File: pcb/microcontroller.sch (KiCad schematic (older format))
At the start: 14 parts, among them J401 JSTA-4, P401 SWD, P402 USB_OTG, SW401 SPST, U401 STM32F072CBT6

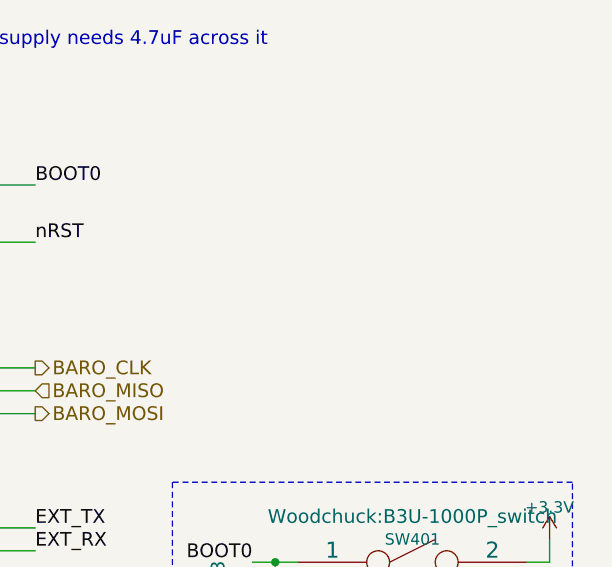
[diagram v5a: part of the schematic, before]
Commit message: Add 24AA01 EEPROM and add agg-kicad library
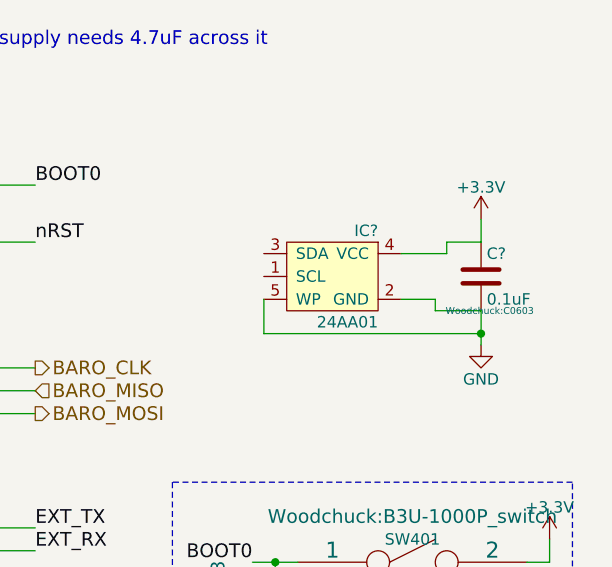
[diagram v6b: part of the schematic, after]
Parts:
- added C?: 0.1uF, Woodchuck:C0603, symbol C
- added IC?: 24AA01, agg:SOT-23-5, symbol 24AA01
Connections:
- net +3V3: now also C?.1, IC?.4 (VCC)
- net GND: now also C?.2, IC?.2 (GND), IC?.5 (WP)
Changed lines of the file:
@@
 LIBS:sma
 LIBS:cga0402mlc-12g
+LIBS:agg-kicad
 LIBS:woodchuck-cache
 EELAYER 25 0
@@
 Text HLabel 6900 4900 2    60   Output ~ 0
 MTX2_P0
+$Comp
+L 24AA01 IC?
+U 1 1 56BF54E5
+P 8200 3500
+F 0 "IC?" H 8000 3700 50  0000 L CNN
+F 1 "24AA01" H 8000 3300 50  0000 L CNN
+F 2 "agg:SOT-23-5" H 8000 3200 50  0001 L CNN
+F 3 "http://ww1.microchip.com/downloads/en/DeviceDoc/21711c.pdf" H 8000 3100 50  0001 L CNN
+F 4 "1331269" H 8000 3000 50  0001 L CNN "Farnell"
+	1    8200 3500
+	-1   0    0    -1
+$EndComp
+$Comp
+L C C?
+U 1 1 56BF5C75
+P 8850 3500
+F 0 "C?" H 8875 3600 50  0000 L CNN
+F 1 "0.1uF" H 8875 3400 50  0000 L CNN
+F 2 "Woodchuck:C0603" H 8888 3350 30  0000 C CNN
+F 3 "" H 8850 3500 60  0000 C CNN
+F 4 "Value" H 8850 3500 60  0001 C CNN "Digikey"
+F 5 "9406140" H 8850 3500 60  0001 C CNN "Farnell"
+F 6 "Value" H 8850 3500 60  0001 C CNN "Fieldname"
+	1    8850 3500
+	1    0    0    -1
+$EndComp
+Wire Wire Line
+	8500 3400 8700 3400
+Wire Wire Line
+	8700 3400 8700 3350
+Wire Wire Line
+	8700 3350 8850 3350
+Wire Wire Line
+	8500 3600 8650 3600
+Wire Wire Line
+	8650 3600 8650 3650
+Wire Wire Line
+	8650 3650 8850 3650
+$Comp
+L GND #PWR?
+U 1 1 56BF61FD
+P 8850 3800
+F 0 "#PWR?" H 8850 3550 50  0001 C CNN
+F 1 "GND" H 8850 3650 50  0000 C CNN
+F 2 "" H 8850 3800 60  0000 C CNN
+F 3 "" H 8850 3800 60  0000 C CNN
+	1    8850 3800
+	1    0    0    -1
+$EndComp
+Wire Wire Line
+	8850 3650 8850 3800
+$Comp
+L +3.3V #PWR?
+U 1 1 56BF6515
+P 8850 3250
+F 0 "#PWR?" H 8850 3100 50  0001 C CNN
+F 1 "+3.3V" H 8850 3390 50  0000 C CNN
+F 2 "" H 8850 3250 50  0000 C CNN
+F 3 "" H 8850 3250 50  0000 C CNN
+	1    8850 3250
+	1    0    0    -1
+$EndComp
+Wire Wire Line
+	8850 3350 8850 3250
+Wire Wire Line
+	8850 3750 7900 3750
+Wire Wire Line
+	7900 3750 7900 3600
+Connection ~ 8850 3750
 $EndSCHEMATC

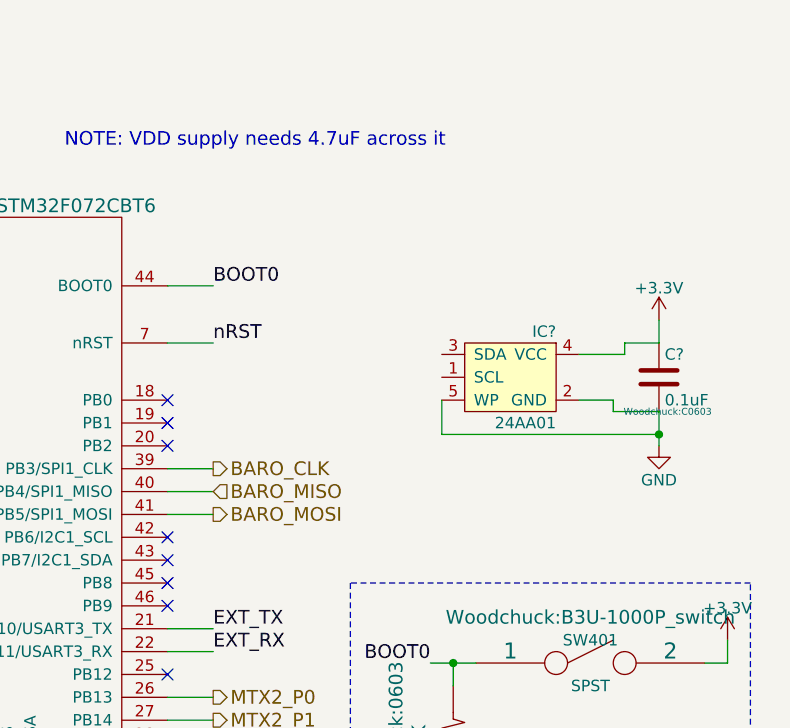
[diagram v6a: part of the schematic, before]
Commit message: Add I2C pull-up resistors
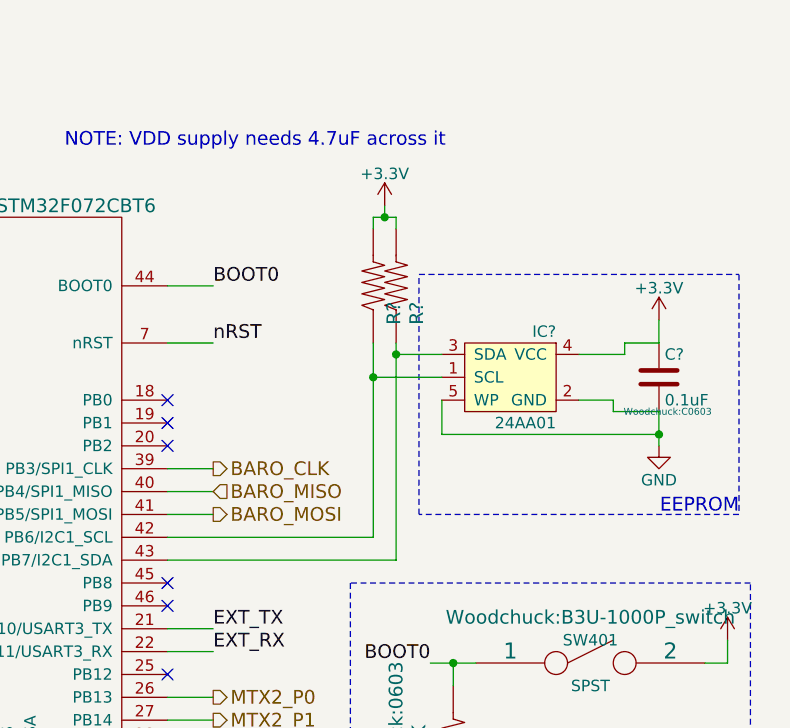
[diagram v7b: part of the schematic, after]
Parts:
- added R? (x2): 10K, Woodchuck:0603, symbol RESISTOR
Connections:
- net +3V3: now also R?.1, R?.1
- net at U401.42 (PB6/I2C1_SCL): now also IC?.1 (SCL), R?.2
- net at U401.43 (PB7/I2C1_SDA): now also IC?.3 (SDA), R?.2
- no-connect marks 23 -> 21
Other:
- note added: "EEPROM"
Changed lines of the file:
@@
 NoConn ~ 6700 3700
 NoConn ~ 6700 3800
-NoConn ~ 6700 4200
-NoConn ~ 6700 4300
 NoConn ~ 6700 4400
 NoConn ~ 6700 4500
@@
 	7900 3750 7900 3600
 Connection ~ 8850 3750
+Wire Wire Line
+	7600 4200 6700 4200
+Wire Wire Line
+	7600 3350 7600 4200
+Wire Wire Line
+	7600 3500 7900 3500
+Wire Wire Line
+	7900 3400 7700 3400
+Wire Wire Line
+	7700 3350 7700 4300
+Wire Wire Line
+	7700 4300 6700 4300
+Wire Notes Line
+	7800 3050 9200 3050
+Wire Notes Line
+	9200 3050 9200 4100
+Wire Notes Line
+	9200 4100 7800 4100
+Wire Notes Line
+	7800 4100 7800 3050
+Text Notes 9200 4100 2    60   ~ 0
+EEPROM
+$Comp
+L RESISTOR R?
+U 1 1 56BF98C6
+P 7700 3100
+F 0 "R?" H 7820 3190 60  0000 C CNN
+F 1 "10K" H 7700 2950 60  0001 C CNN
+F 2 "Woodchuck:0603" H 7700 3100 60  0001 C CNN
+F 3 "" H 7700 3100 60  0000 C CNN
+F 4 "Value" H 7700 3100 60  0001 C CNN "Digikey"
+F 5 "1469826" H 7700 3100 60  0001 C CNN "Farnell"
+F 6 "Value" H 7700 3100 60  0001 C CNN "Fieldname"
+	1    7700 3100
+	0    1    1    0
+$EndComp
+Connection ~ 7700 3400
+$Comp
+L RESISTOR R?
+U 1 1 56BF9EA2
+P 7600 3100
+F 0 "R?" H 7720 3190 60  0000 C CNN
+F 1 "10K" H 7600 2950 60  0001 C CNN
+F 2 "Woodchuck:0603" H 7600 3100 60  0001 C CNN
+F 3 "" H 7600 3100 60  0000 C CNN
+F 4 "Value" H 7600 3100 60  0001 C CNN "Digikey"
+F 5 "1469826" H 7600 3100 60  0001 C CNN "Farnell"
+F 6 "Value" H 7600 3100 60  0001 C CNN "Fieldname"
+	1    7600 3100
+	0    1    1    0
+$EndComp
+Connection ~ 7600 3500
+Wire Wire Line
+	7600 2850 7600 2800
+Wire Wire Line
+	7600 2800 7700 2800
+Wire Wire Line
+	7700 2800 7700 2850
+$Comp
+L +3.3V #PWR?
+U 1 1 56BFA35F
+P 7650 2750
+F 0 "#PWR?" H 7650 2600 50  0001 C CNN
+F 1 "+3.3V" H 7650 2890 50  0000 C CNN
+F 2 "" H 7650 2750 50  0000 C CNN
+F 3 "" H 7650 2750 50  0000 C CNN
+	1    7650 2750
+	1    0    0    -1
+$EndComp
+Wire Wire Line
+	7650 2750 7650 2800
+Connection ~ 7650 2800
 $EndSCHEMATC

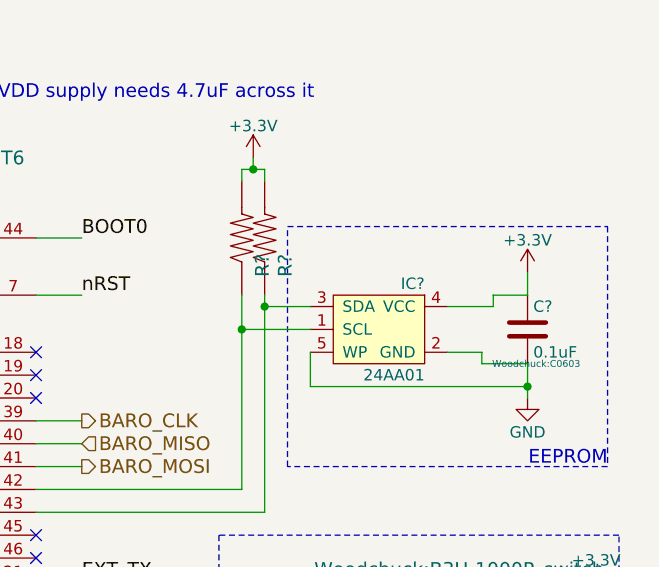
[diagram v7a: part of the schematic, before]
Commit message: Ran ERC and regenerated netlist
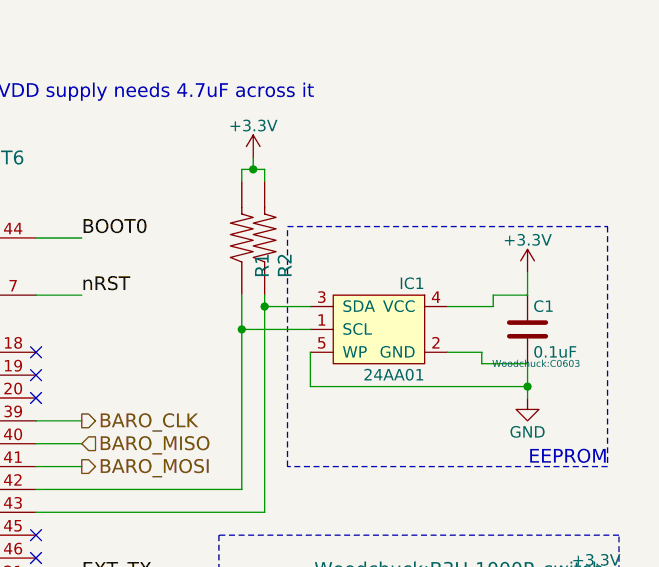
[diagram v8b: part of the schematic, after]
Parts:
- gave numbers to parts that had none: 4
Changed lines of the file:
@@
 MTX2_P0
 $Comp
-L 24AA01 IC?
+L 24AA01 IC1
 U 1 1 56BF54E5
 P 8200 3500
-F 0 "IC?" H 8000 3700 50  0000 L CNN
+F 0 "IC1" H 8000 3700 50  0000 L CNN
 F 1 "24AA01" H 8000 3300 50  0000 L CNN
 F 2 "agg:SOT-23-5" H 8000 3200 50  0001 L CNN
@@
 $EndComp
 $Comp
-L C C?
+L C C1
 U 1 1 56BF5C75
 P 8850 3500
-F 0 "C?" H 8875 3600 50  0000 L CNN
+F 0 "C1" H 8875 3600 50  0000 L CNN
 F 1 "0.1uF" H 8875 3400 50  0000 L CNN
 F 2 "Woodchuck:C0603" H 8888 3350 30  0000 C CNN
@@
 	8650 3650 8850 3650
 $Comp
-L GND #PWR?
+L GND #PWR030
 U 1 1 56BF61FD
 P 8850 3800
-F 0 "#PWR?" H 8850 3550 50  0001 C CNN
+F 0 "#PWR030" H 8850 3550 50  0001 C CNN
 F 1 "GND" H 8850 3650 50  0000 C CNN
 F 2 "" H 8850 3800 60  0000 C CNN
@@
 	8850 3650 8850 3800
 $Comp
-L +3.3V #PWR?
+L +3.3V #PWR031
 U 1 1 56BF6515
 P 8850 3250
-F 0 "#PWR?" H 8850 3100 50  0001 C CNN
+F 0 "#PWR031" H 8850 3100 50  0001 C CNN
 F 1 "+3.3V" H 8850 3390 50  0000 C CNN
 F 2 "" H 8850 3250 50  0000 C CNN
@@
 EEPROM
 $Comp
-L RESISTOR R?
+L RESISTOR R2
 U 1 1 56BF98C6
 P 7700 3100
-F 0 "R?" H 7820 3190 60  0000 C CNN
+F 0 "R2" H 7820 3190 60  0000 C CNN
 F 1 "10K" H 7700 2950 60  0001 C CNN
 F 2 "Woodchuck:0603" H 7700 3100 60  0001 C CNN
@@
 Connection ~ 7700 3400
 $Comp
-L RESISTOR R?
+L RESISTOR R1
 U 1 1 56BF9EA2
 P 7600 3100
-F 0 "R?" H 7720 3190 60  0000 C CNN
+F 0 "R1" H 7720 3190 60  0000 C CNN
 F 1 "10K" H 7600 2950 60  0001 C CNN
 F 2 "Woodchuck:0603" H 7600 3100 60  0001 C CNN
@@
 	7700 2800 7700 2850
 $Comp
-L +3.3V #PWR?
+L +3.3V #PWR032
 U 1 1 56BFA35F
 P 7650 2750
-F 0 "#PWR?" H 7650 2600 50  0001 C CNN
+F 0 "#PWR032" H 7650 2600 50  0001 C CNN
 F 1 "+3.3V" H 7650 2890 50  0000 C CNN
 F 2 "" H 7650 2750 50  0000 C CNN
